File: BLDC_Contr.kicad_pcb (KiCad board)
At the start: 4 copper layers, 90 x 60.4 mm, 100 parts, among them J1 XT60, J10 PH, J2 Conn_ARM_SWD_TagConnect_TC2030, J3 PH, J4 PH, J5 PH, J6 PH, J7 PH, J8 PIN, Q1 CSD18540Q5B, Q2 CSD18540Q5B, Q3 CSD18540Q5B, Q4 CSD18540Q5B, Q5 CSD18540Q5B, Q6 CSD18540Q5B, U1 STM32G431CBU6, U2 DRV8323RSRGZR, U3 AMS1117-3.3, Y1 Crystal_16Mhz

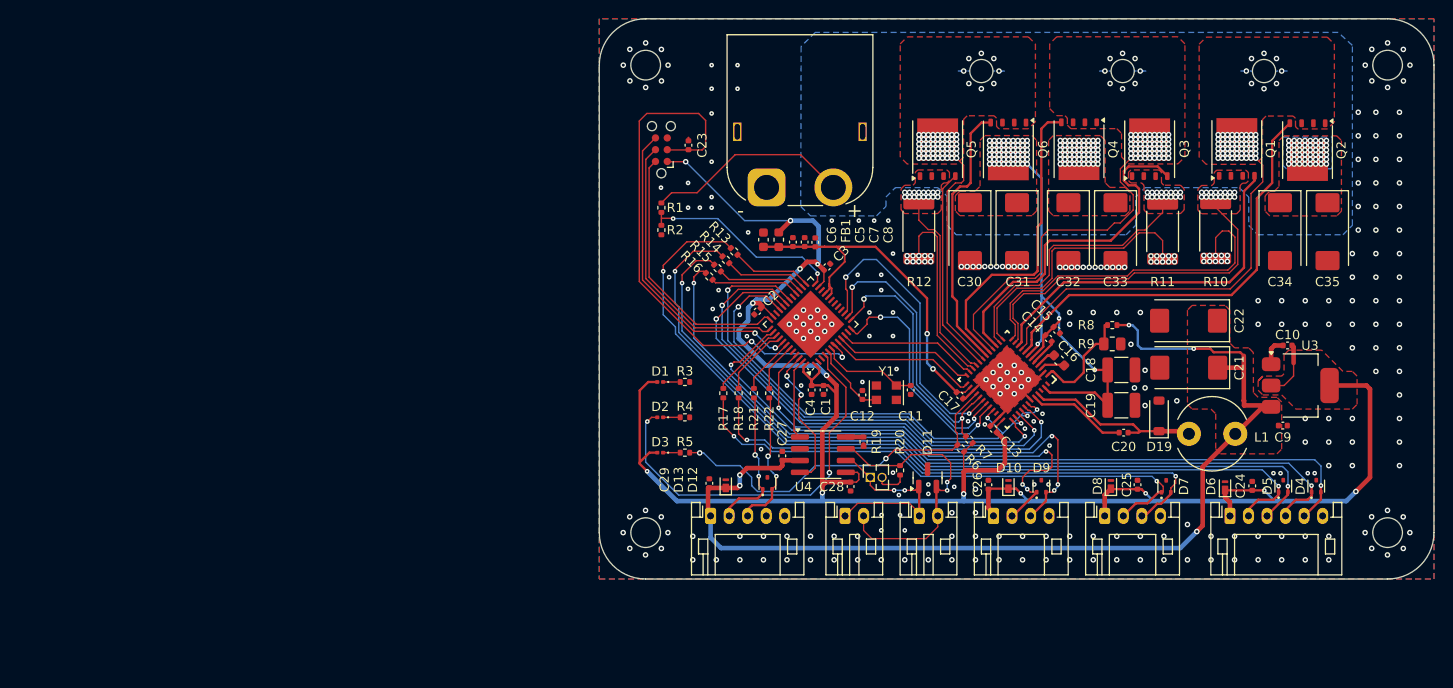
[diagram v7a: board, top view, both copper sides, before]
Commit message: pcb gerber made. checking for errors. add gnd vias
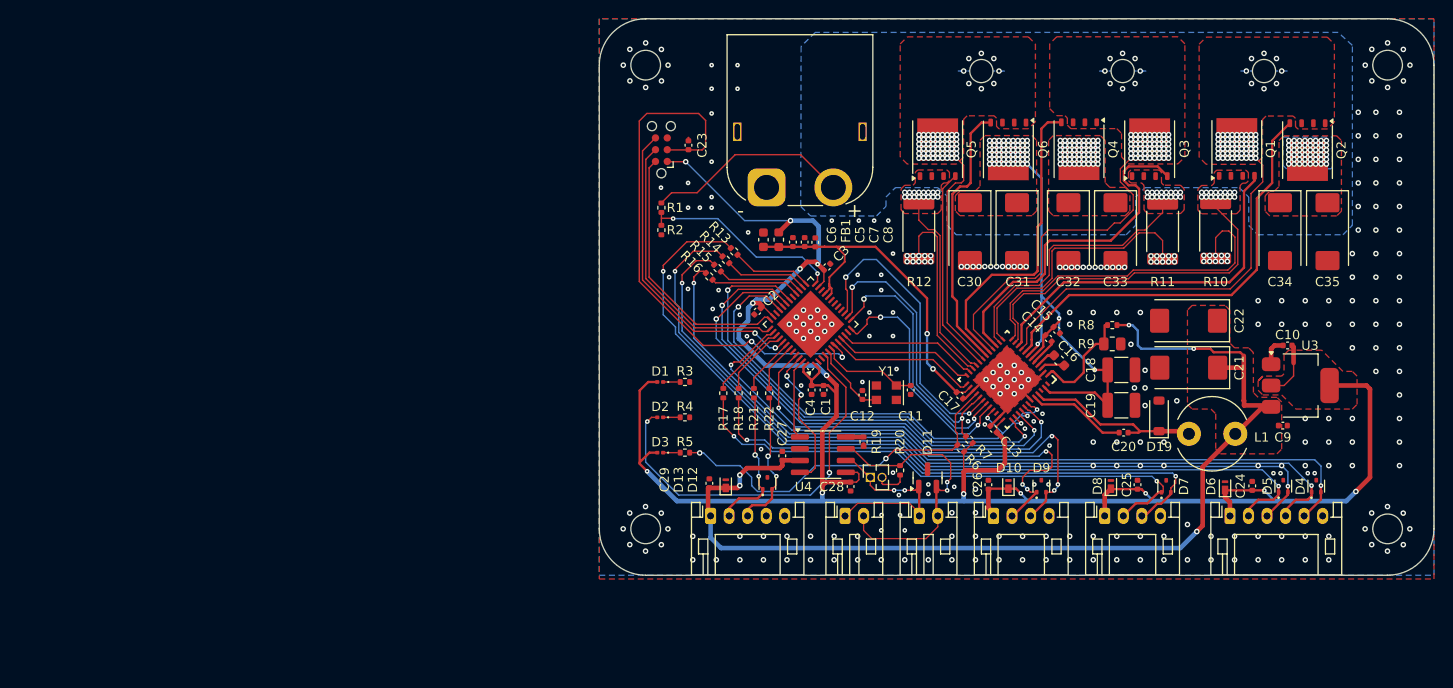
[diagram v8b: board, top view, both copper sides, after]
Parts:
- moved H3 0.41 mm to (91.1, 79.6)
- moved H4 0.41 mm to (171.1, 79.6)
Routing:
- net GND: vias 291 -> 302
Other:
- board size 90 x 60.4 mm -> 90 x 60 mm
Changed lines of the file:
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@@
 			(outputformat 1)
 			(mirror no)
-			(drillshape 1)
+			(drillshape 0)
 			(scaleselection 1)
 			(outputdirectory "")
@@
 		(locked yes)
 		(layer "F.Cu")
-		(at 91.059183 80)
+		(at 91.059183 79.592904)
 		(descr "Mounting Hole 3.2mm, M3, no annular, generated by kicad-footprint-generator mountinghole.py")
 		(tags "mountinghole M3")
@@
 		(locked yes)
 		(layer "F.Cu")
-		(at 171.059184 80)
+		(at 171.059184 79.592904)
 		(descr "Mounting Hole 3.2mm, M3, no annular, generated by kicad-footprint-generator mountinghole.py")
 		(tags "mountinghole M3")
@@
 	(gr_line
 		(start 176.059184 29.592904)
-		(end 176.059184 80)
+		(end 176.059183 79.592904)
 		(stroke
 			(width 0.05)
@@
 	)
 	(gr_arc
-		(start 91.059183 85)
-		(mid 87.523649 83.535534)
-		(end 86.059183 80)
+		(start 91.059183 84.592921)
+		(mid 87.523648 83.128444)
+		(end 86.059183 79.592904)
 		(stroke
 			(width 0.05)
 			(type default)
 		)
+		(locked yes)
 		(layer "Edge.Cuts")
 	)
@@
 	)
 	(gr_line
-		(start 86.059183 80)
+		(start 86.059183 79.592904)
 		(end 86.059183 29.592904)
 		(stroke
@@
 	)
 	(gr_arc
-		(start 176.059184 80)
-		(mid 174.594717 83.535528)
-		(end 171.059184 85)
+		(start 176.059166 79.592904)
+		(mid 174.594699 83.128432)
+		(end 171.059167 84.592887)
 		(stroke
 			(width 0.05)
@@
 	)
 	(gr_line
-		(start 171.059184 85)
-		(end 91.059183 85)
+		(start 171.059184 84.592904)
+		(end 91.059183 84.592904)
 		(stroke
 			(width 0.05)
@@
 	)
 	(via
-		(at 171.046183 82.403001)
+		(at 171.046183 81.995905)
 		(size 0.6)
 		(drill 0.3)
 		(layers "F.Cu" "B.Cu")
+		(locked yes)
 		(net 85)
 	)
@@
 	)
 	(via
+		(at 141.859183 72.772904)
+		(size 0.6)
+		(drill 0.3)
+		(layers "F.Cu" "B.Cu")
+		(net 85)
+	)
+	(via
 		(at 136.779183 56.262904)
 		(size 0.6)
@@
 	)
 	(via
+		(at 159.639183 72.772904)
+		(size 0.6)
+		(drill 0.3)
+		(layers "F.Cu" "B.Cu")
+		(net 85)
+	)
+	(via
+		(at 162.179183 72.772904)
+		(size 0.6)
+		(drill 0.3)
+		(layers "F.Cu" "B.Cu")
+		(net 85)
+	)
+	(via
 		(at 139.319183 82.932904)
 		(size 0.6)
@@
 	)
 	(via
+		(at 139.319183 70.232904)
+		(size 0.6)
+		(drill 0.3)
+		(layers "F.Cu" "B.Cu")
+		(net 85)
+	)
+	(via
 		(at 162.179183 82.932904)
 		(size 0.6)
@@
 	)
 	(via
+		(at 146.939183 72.772904)
+		(size 0.6)
+		(drill 0.3)
+		(layers "F.Cu" "B.Cu")
+		(net 85)
+	)
+	(via
 		(at 131.699183 82.932904)
 		(size 0.6)
@@
 	)
 	(via
+		(at 144.399183 70.232904)
+		(size 0.6)
+		(drill 0.3)
+		(layers "F.Cu" "B.Cu")
+		(net 85)
+	)
+	(via
 		(at 172.339183 72.772904)
 		(size 0.6)
@@
 	)
 	(via
-		(at 92.743239 78.302944)
+		(at 92.743239 77.895848)
 		(size 0.6)
 		(drill 0.3)
 		(layers "F.Cu" "B.Cu")
+		(locked yes)
 		(net 85)
 	)
@@
 	)
 	(via
-		(at 91.046183 82.403001)
+		(at 91.046183 81.995905)
 		(size 0.6)
 		(drill 0.3)
 		(layers "F.Cu" "B.Cu")
+		(locked yes)
 		(net 85)
 	)
@@
 	)
 	(via
-		(at 91.046183 77.6)
+		(at 91.046183 77.192904)
 		(size 0.6)
 		(drill 0.3)
 		(layers "F.Cu" "B.Cu")
+		(locked yes)
 		(net 85)
 	)
@@
 	)
 	(via
-		(at 168.633183 80)
+		(at 168.633183 79.592904)
+		(size 0.6)
+		(drill 0.3)
+		(layers "F.Cu" "B.Cu")
+		(locked yes)
+		(net 85)
+	)
+	(via
+		(at 173.459183 79.592904)
 		(size 0.6)
 		(drill 0.3)
 		(layers "F.Cu" "B.Cu")
+		(locked yes)
 		(net 85)
 	)
 	(via
-		(at 173.459183 80)
+		(at 157.099183 72.772904)
 		(size 0.6)
 		(drill 0.3)
@@
 	)
 	(via
-		(at 171.046183 77.6)
+		(at 171.046183 77.192904)
 		(size 0.6)
 		(drill 0.3)
 		(layers "F.Cu" "B.Cu")
+		(locked yes)
 		(net 85)
 	)
@@
 	)
 	(via
-		(at 89.339934 78.293751)
+		(at 89.339934 77.886655)
 		(size 0.6)
 		(drill 0.3)
 		(layers "F.Cu" "B.Cu")
+		(locked yes)
 		(net 85)
 	)
 	(via
-		(at 89.347005 81.699178)
+		(at 89.347005 81.292082)
 		(size 0.6)
 		(drill 0.3)
 		(layers "F.Cu" "B.Cu")
+		(locked yes)
 		(net 85)
 	)
@@
 	)
 	(via
-		(at 169.339934 78.293751)
+		(at 169.339934 77.886655)
 		(size 0.6)
 		(drill 0.3)
 		(layers "F.Cu" "B.Cu")
+		(locked yes)
 		(net 85)
 	)
@@
 	)
 	(via
-		(at 172.743239 78.302944)
+		(at 172.743239 77.895848)
 		(size 0.6)
 		(drill 0.3)
 		(layers "F.Cu" "B.Cu")
+		(locked yes)
 		(net 85)
 	)
@@
 	)
 	(via
-		(at 93.459183 80)
+		(at 93.459183 79.592904)
 		(size 0.6)
 		(drill 0.3)
 		(layers "F.Cu" "B.Cu")
+		(locked yes)
 		(net 85)
 	)
@@
 	)
 	(via
+		(at 146.939183 70.232904)
+		(size 0.6)
+		(drill 0.3)
+		(layers "F.Cu" "B.Cu")
+		(net 85)
+	)
+	(via
 		(at 151.241784 50.116104)
 		(size 0.6)
@@
 	)
 	(via
-		(at 172.752432 81.706249)
+		(at 172.752432 81.299153)
 		(size 0.6)
 		(drill 0.3)
 		(layers "F.Cu" "B.Cu")
+		(locked yes)
 		(net 85)
 	)
@@
 	)
 	(via
-		(at 88.633183 80)
+		(at 88.633183 79.592904)
 		(size 0.6)
 		(drill 0.3)
 		(layers "F.Cu" "B.Cu")
+		(locked yes)
 		(net 85)
 	)
@@
 	)
 	(via
-		(at 92.752432 81.706249)
+		(at 92.752432 81.299153)
 		(size 0.6)
 		(drill 0.3)
 		(layers "F.Cu" "B.Cu")
+		(locked yes)
 		(net 85)
 	)
@@
 	)
 	(via
+		(at 141.859183 70.232904)
+		(size 0.6)
+		(drill 0.3)
+		(layers "F.Cu" "B.Cu")
+		(net 85)
+	)
+	(via
 		(at 100.965183 29.592904)
 		(size 0.5)
@@
 	)
 	(via
+		(at 144.399183 72.772904)
+		(size 0.6)
+		(drill 0.3)
+		(layers "F.Cu" "B.Cu")
+		(net 85)
+	)
+	(via
 		(at 96.901183 44.959904)
 		(size 0.5)
@@
 	)
 	(via
-		(at 169.347005 81.699178)
+		(at 169.347005 81.292082)
 		(size 0.6)
 		(drill 0.3)
 		(layers "F.Cu" "B.Cu")
+		(locked yes)
 		(net 85)
 	)
@@
 	)
 	(via
+		(at 139.319183 72.772904)
+		(size 0.6)
+		(drill 0.3)
+		(layers "F.Cu" "B.Cu")
+		(net 85)
+	)
+	(via
 		(at 154.559183 80.392904)
 		(size 0.6)
@@
 		(polygon
 			(pts
-				(xy 86.059183 24.592904) (xy 86.059183 85) (xy 176.059184 85) (xy 176.059184 24.592904)
+				(xy 86.059183 24.592904) (xy 86.059183 84.592904) (xy 176.059184 84.592904) (xy 176.059184 24.592904)
 			)
 		)
@@
 	)
 	(group ""
-		(members "015bc96d-52ae-4237-9cea-c803cdc060c8" "5c3149a8-534f-449f-af08-2477fa4599a0"
-			"5c898a15-3fd5-42a1-b1ce-b0aa2cb81f6f" "60a6d9c5-4e0c-47e5-a6c4-2b91bd316f5e"
-			"75fd0c8a-d1b3-4d03-87cf-4c3295391784" "910b1ba7-a961-4568-9e4e-3d8d874c7896"
-			"aef2b7fb-cbc2-422a-8e7b-cb6b81c2f745" "f908de52-3760-40b9-a6c7-80a8922a0b1f"
-		)
-	)
-	(group ""
+		(locked yes)
 		(members "477ea63f-5f2d-488a-a8b6-437bcb70cf9b" "5155129c-d2ec-4545-b74b-992512748638"
 			"590e4e27-a645-44fb-a2c0-75bc173ef39c" "6a373e26-43ed-4ba9-a6d9-20959728a758"
@@
 		)
 	)
+	(group ""
+		(locked yes)
+		(members "76a6c147-e04c-42ba-b8ba-ae9ad6065b0f" "a41f7b5c-d24f-4aa9-940b-305641e37b43")
+	)
+	(group ""
+		(locked yes)
+		(members "015bc96d-52ae-4237-9cea-c803cdc060c8" "5c3149a8-534f-449f-af08-2477fa4599a0"
+			"5c898a15-3fd5-42a1-b1ce-b0aa2cb81f6f" "60a6d9c5-4e0c-47e5-a6c4-2b91bd316f5e"
+			"7399f411-6158-4d25-872f-363c1381411d" "75fd0c8a-d1b3-4d03-87cf-4c3295391784"
+			"910b1ba7-a961-4568-9e4e-3d8d874c7896" "aef2b7fb-cbc2-422a-8e7b-cb6b81c2f745"
+			"cf056b7b-bd00-4ecf-863d-44aab3420e8d" "f908de52-3760-40b9-a6c7-80a8922a0b1f"
+		)
+	)
